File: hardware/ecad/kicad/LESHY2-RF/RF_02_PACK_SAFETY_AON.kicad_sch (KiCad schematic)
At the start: 0 parts

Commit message: complete exact H2.3.1 RF power hierarchy
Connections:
- no-connect marks 0 -> 7
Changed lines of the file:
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@@
 	(generator_version "10.0")
 	(paper "A4")
+	(hierarchical_label "PACK_ADMISSION_VDD"
+		(shape bidirectional)
+		(at 20.32 20.32 0)
+		(effects (font (size 1.27 1.27)))
+	)
+	(wire
+		(pts (xy 20.32 20.32) (xy 25.40 20.32))
+		(stroke (width 0) (type default))
+	)
+	(no_connect (at 25.40 20.32)
+	)
+	(hierarchical_label "POWER_COMMAND_OFF_N"
+		(shape bidirectional)
+		(at 20.32 25.40 0)
+		(effects (font (size 1.27 1.27)))
+	)
+	(wire
+		(pts (xy 20.32 25.40) (xy 25.40 25.40))
+		(stroke (width 0) (type default))
+	)
+	(no_connect (at 25.40 25.40)
+	)
+	(hierarchical_label "POWER_GROUND"
+		(shape bidirectional)
+		(at 20.32 30.48 0)
+		(effects (font (size 1.27 1.27)))
+	)
+	(wire
+		(pts (xy 20.32 30.48) (xy 25.40 30.48))
+		(stroke (width 0) (type default))
+	)
+	(no_connect (at 25.40 30.48)
+	)
+	(hierarchical_label "PROTECTED_PACK_POSITIVE"
+		(shape bidirectional)
+		(at 20.32 35.56 0)
+		(effects (font (size 1.27 1.27)))
+	)
+	(wire
+		(pts (xy 20.32 35.56) (xy 25.40 35.56))
+		(stroke (width 0) (type default))
+	)
+	(no_connect (at 25.40 35.56)
+	)
+	(hierarchical_label "SYS_I2C_SCL"
+		(shape bidirectional)
+		(at 190.50 20.32 180)
+		(effects (font (size 1.27 1.27)) (justify right))
+	)
+	(wire
+		(pts (xy 190.50 20.32) (xy 185.42 20.32))
+		(stroke (width 0) (type default))
+	)
+	(no_connect (at 185.42 20.32)
+	)
+	(hierarchical_label "SYS_I2C_SDA"
+		(shape bidirectional)
+		(at 190.50 25.40 180)
+		(effects (font (size 1.27 1.27)) (justify right))
+	)
+	(wire
+		(pts (xy 190.50 25.40) (xy 185.42 25.40))
+		(stroke (width 0) (type default))
+	)
+	(no_connect (at 185.42 25.40)
+	)
+	(hierarchical_label "SYS_INT_N"
+		(shape bidirectional)
+		(at 190.50 30.48 180)
+		(effects (font (size 1.27 1.27)) (justify right))
+	)
+	(wire
+		(pts (xy 190.50 30.48) (xy 185.42 30.48))
+		(stroke (width 0) (type default))
+	)
+	(no_connect (at 185.42 30.48)
+	)
 	(sheet_instances
 		(path "/"

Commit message: complete exact H2.3.3 pack safety
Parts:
- added BT1: Keystone Electronics 1048P, Leshy2:Keystone-1048P, symbol Leshy2:RF02_PACK_HOLDER
- added BT2: XTAR 18650 4000mAh, symbol Leshy2:RF02_PACK_CELL0
- added BT3: XTAR 18650 4000mAh, symbol Leshy2:RF02_PACK_CELL1
- added C1: TDK C1005X7R1H104K050BB, Capacitor_SMD:C_0402_1005Metric, symbol Leshy2:RF02_PACK_IN_BYPASS
- added C10: Murata GRM188R60J106ME47D, Capacitor_SMD:C_0603_1608Metric, symbol Leshy2:RF02_PACK_ADMISSION_BULK_CAP
- added C11: TDK C1005X7R1H104K050BB, Capacitor_SMD:C_0402_1005Metric, symbol Leshy2:RF02_PACK_ADMISSION_BYPASS
- added C12: Murata GRM155R71H103KA88D, Capacitor_SMD:C_0402_1005Metric, symbol Leshy2:RF02_PACK_ADMISSION_RESET_CAP
- added C13: Murata GRM31C5C1H224JE02L, Capacitor_SMD:C_1206_3216Metric, symbol Leshy2:RF02_PACK_DIAG_TIMER_CAP
- added C14: TDK C1608X7R1C105K080AC, Capacitor_SMD:C_0603_1608Metric, symbol Leshy2:RF02_PACK_DIAG_LOCKOUT_CAP
- added C15: TDK C1005X7R1H104K050BB, Capacitor_SMD:C_0402_1005Metric, symbol Leshy2:RF02_PACK_DIAG_TIMER_BYPASS
- added C16: Murata GRM155R71H103KA88D, Capacitor_SMD:C_0402_1005Metric, symbol Leshy2:RF02_PACK_MID_ADC_FILTER
- added C17: Murata GRM155R71H103KA88D, Capacitor_SMD:C_0402_1005Metric, symbol Leshy2:RF02_PACK_STACK_ADC_FILTER
- added C2: Murata GRM188R71E474KA12D, Capacitor_SMD:C_0603_1608Metric, symbol Leshy2:RF02_PACK_CP_CAP
- added C3: TDK C1005X7R1H104K050BB, Capacitor_SMD:C_0402_1005Metric, symbol Leshy2:RF02_PACK_CHG_GATE_CAP
- added C4: TDK C1005X7R1H104K050BB, Capacitor_SMD:C_0402_1005Metric, symbol Leshy2:RF02_PACK_DIS_GATE_CAP
- added C5: Murata GRM188R71E474KA12D, Capacitor_SMD:C_0603_1608Metric, symbol Leshy2:RF02_PACK_AOLDO_CAP
- added C6: Murata GRM188R71E474KA12D, Capacitor_SMD:C_0603_1608Metric, symbol Leshy2:RF02_PACK_REG3_CAP
- added C7: Murata GRM188R71E474KA12D, Capacitor_SMD:C_0603_1608Metric, symbol Leshy2:RF02_PACK_REG2_CAP
- added C8: TDK C1005X7R1H104K050BB, Capacitor_SMD:C_0402_1005Metric, symbol Leshy2:RF02_PACK_CELL1_FILTER_CAP
- added C9: TDK C1005X7R1H104K050BB, Capacitor_SMD:C_0402_1005Metric, symbol Leshy2:RF02_PACK_BATTS_FILTER_CAP
- added D1: onsemi BAV70LT1G, Package_TO_SOT_SMD:SOT-23, symbol Leshy2:RF02_PACK_SUPPLY_OR
- added D2: Diodes Incorporated BAT54-7-F, Package_TO_SOT_SMD:SOT-23, symbol Leshy2:RF02_PACK_SYSTEM_DIODE
- added F1: Littelfuse 0451005.MRL, Leshy2:0451005.MRL, symbol Leshy2:RF02_PACK_FUSE0
- added F2: Littelfuse 0451005.MRL, Leshy2:0451005.MRL, symbol Leshy2:RF02_PACK_FUSE1
- added Q1: Diodes Incorporated 2N7002DW-7-F, Package_TO_SOT_SMD:SOT-363_SC-70-6, symbol Leshy2:RF02_PACK_HOLD
- added Q2: Diodes Incorporated 2N7002DW-7-F, Package_TO_SOT_SMD:SOT-363_SC-70-6, symbol Leshy2:RF02_PACK_STATUS_BUFFER
- added Q3: Diodes Incorporated DMN2056U-7, Package_TO_SOT_SMD:SOT-23, symbol Leshy2:RF02_PACK_DIAG_SWITCH
- added R1: Vishay WSL25125L000FEA, Resistor_SMD:R_2512_6332Metric, symbol Leshy2:RF02_PACK_SHUNT
- added R10: Yageo RC0402FR-071KL, Resistor_SMD:R_0402_1005Metric, symbol Leshy2:RF02_PACK_PCKP_RES
- added R11: Panasonic ERJ-P08F49R9V, Resistor_SMD:R_1206_3216Metric, symbol Leshy2:RF02_PACK_CELL1_RBAL
- added R12: Panasonic ERJ-P08F49R9V, Resistor_SMD:R_1206_3216Metric, symbol Leshy2:RF02_PACK_BATTS_RBAL
- added R13: Yageo RC0402FR-0747KL, Resistor_SMD:R_0402_1005Metric, symbol Leshy2:RF02_PACK_ADMISSION_RESET_PULLUP
- added R14: Yageo RC0402FR-07169KL, Resistor_SMD:R_0402_1005Metric, symbol Leshy2:RF02_PACK_DIAG_TIMER_RES
- added R15: Yageo RC0402FR-07620KL, Resistor_SMD:R_0402_1005Metric, symbol Leshy2:RF02_PACK_DIAG_LOCKOUT_RES
- added R16: Yageo RC0402FR-0710KL, Resistor_SMD:R_0402_1005Metric, symbol Leshy2:RF02_PACK_DIAG_TRIGGER_PULLDOWN
- added R17: Yageo RC0402FR-0710KL, Resistor_SMD:R_0402_1005Metric, symbol Leshy2:RF02_PACK_DIAG_GATE_PULLDOWN
- added R18: Bourns CRM2512-FX-20R0ELF, Resistor_SMD:R_2512_6332Metric, symbol Leshy2:RF02_PACK_DIAG_RES0
- added R19: Bourns CRM2512-FX-20R0ELF, Resistor_SMD:R_2512_6332Metric, symbol Leshy2:RF02_PACK_DIAG_RES1
- added R2: Yageo RC0402FR-0710KL, Resistor_SMD:R_0402_1005Metric, symbol Leshy2:RF02_PACK_HOLD_PULLUP
- added R20: Yageo RC0402FR-07220KL, Resistor_SMD:R_0402_1005Metric, symbol Leshy2:RF02_PACK_MID_ADC_TOP0
- added R21: Yageo RC0402FR-07220KL, Resistor_SMD:R_0402_1005Metric, symbol Leshy2:RF02_PACK_MID_ADC_TOP1
- added R22: Yageo RC0402FR-07169KL, Resistor_SMD:R_0402_1005Metric, symbol Leshy2:RF02_PACK_MID_ADC_BOTTOM
- added R23: Yageo RC0402FR-07220KL, Resistor_SMD:R_0402_1005Metric, symbol Leshy2:RF02_PACK_STACK_ADC_TOP0
- added R24: Yageo RC0402FR-07220KL, Resistor_SMD:R_0402_1005Metric, symbol Leshy2:RF02_PACK_STACK_ADC_TOP1
- added R25: Yageo RC0402FR-07220KL, Resistor_SMD:R_0402_1005Metric, symbol Leshy2:RF02_PACK_STACK_ADC_TOP2
- added R26: Yageo RC0402FR-07220KL, Resistor_SMD:R_0402_1005Metric, symbol Leshy2:RF02_PACK_STACK_ADC_TOP3
- added R27: Yageo RC0402FR-07220KL, Resistor_SMD:R_0402_1005Metric, symbol Leshy2:RF02_PACK_STACK_ADC_TOP4
- added R28: Yageo RC0402FR-07169KL, Resistor_SMD:R_0402_1005Metric, symbol Leshy2:RF02_PACK_STACK_ADC_BOTTOM
- added R3: Yageo RC0402FR-0710KL, Resistor_SMD:R_0402_1005Metric, symbol Leshy2:RF02_PACK_HOLD_RELEASE_PULLDOWN
- added R4: Yageo RC0402FR-0710KL, Resistor_SMD:R_0402_1005Metric, symbol Leshy2:RF02_PACK_ALRT_PULLUP
- added R5: Yageo RC0402FR-0710KL, Resistor_SMD:R_0402_1005Metric, symbol Leshy2:RF02_PACK_PFAIL_PULLUP
- added R6: Yageo RC0402FR-0710KL, Resistor_SMD:R_0402_1005Metric, symbol Leshy2:RF02_PACK_IRQ_GATE_PULLDOWN
- added R7: Yageo RC0402FR-0710KL, Resistor_SMD:R_0402_1005Metric, symbol Leshy2:RF02_PACK_GAUGE_SCL_PULLUP
- added R8: Yageo RC0402FR-0710KL, Resistor_SMD:R_0402_1005Metric, symbol Leshy2:RF02_PACK_GAUGE_SDA_PULLUP
- added R9: Panasonic ERJ-P08F10R0V, Resistor_SMD:R_1206_3216Metric, symbol Leshy2:RF02_PACK_IN_RES
- added RT1: TDK B57332V5103F360, Capacitor_SMD:C_0603_1608Metric, symbol Leshy2:RF02_PACK_NTC0
- added RT2: TDK B57332V5103F360, Capacitor_SMD:C_0603_1608Metric, symbol Leshy2:RF02_PACK_NTC1
- added U1: Analog Devices MAX17320G20+T, Package_DFN_QFN:TQFN-24-1EP_4x4mm_P0.5mm_EP2.6x2.6mm, symbol Leshy2:RF02_PACK_GAUGE
- added U2: Texas Instruments MSPM0C1106SDGS20R, Package_SO:Texas_DGS0020A_TSSOP-20_3x5.1mm_P0.5mm, symbol Leshy2:RF02_PACK_ADMISSION
- added U3: Texas Instruments CSD87313DMST, Leshy2:CSD87313DMST, symbol Leshy2:RF02_PACK_POWER_FET
- added U4: Texas Instruments TPUL2G223BQBR, Leshy2:TPUL2G223BQBR, symbol Leshy2:RF02_PACK_DIAG_TIMER
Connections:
- net PACK_ADMISSION_VDD: now also C10.1 (END_1), C11.1 (END_1), C15.1 (END_1), D1.3 (K_COMMON), D2.3 (K), R13.1 (END_1), R14.1 (END_1), R15.1 (END_1), R5.1 (END_1), R7.1 (END_1), R8.1 (END_1), U2.6 (VDD), U4.10 (CH2_T), U4.11 (CH2_CLR_N), U4.16 (VCC)
- net POWER_COMMAND_OFF_N: now also U2.19 (PA24)
- net POWER_GROUND: now also R1.2 (END_2), U1.14 (CSN)
- net PROTECTED_PACK_POSITIVE: now also C4.2 (END_2), R10.2 (END_2), U3.5 (S2_5), U3.6 (S2_6)
- net SYS_I2C_SCL: now also U2.11 (PA11)
- net SYS_I2C_SDA: now also U2.4 (PA0)
- net SYS_INT_N: now also Q2.1 (D2)
- new net 3V3_MAIN: D2.1 (A)
- new net BATTERY_STACK_POSITIVE: C3.2 (END_2), F2.2 (END_2), R12.1 (END_1), R18.1 (END_1), R19.1 (END_1), R23.1 (END_1), R9.1 (END_1), U3.7 (S1_7), U3.8 (S1_8)
- new net PACK_2S_MIDPOINT: BT1.4 (SLOT1_NEG), BT3.2 (NEG), F1.2 (END_2), R11.1 (END_1), R20.1 (END_1)
- new net PACK_ADMISSION_NRST_N: C12.1 (END_1), R13.2 (END_2), U2.5 (PA1_NRST)
- new net PACK_ADMISSION_SWCLK: U2.16 (PA20_SWCLK)
- new net PACK_ADMISSION_SWDIO: U2.15 (PA19_SWDIO)
- new net PACK_ADMISSION_UART_RX: U2.14 (PA18)
- new net PACK_ADMISSION_UART_TX: U2.13 (PA17)
- new net PACK_AOLDO: C5.1 (END_1), D1.1 (A1), R2.1 (END_1), U1.12 (AOLDO)
- new net PACK_BATTS_SENSE: C9.1 (END_1), R12.2 (END_2), U1.24 (BATTS)
- new net PACK_CELL0_ADC: C16.1 (END_1), R21.2 (END_2), R22.1 (END_1), U2.20 (PA25)
- new net PACK_CELL0_TEMP: RT1.1 (END_1), U1.10 (TH1)
- new net PACK_CELL1_SENSE: C8.1 (END_1), C9.2 (END_2), R11.2 (END_2), U1.21 (CELL1), U1.22 (CELL2), U1.23 (CELL3)
- new net PACK_CELL1_TEMP: RT2.1 (END_1), U1.16 (TH2)
- new net PACK_CHARGE_PUMP: C2.1 (END_1), U1.2 (CP)
- new net PACK_CHG_GATE: C3.1 (END_1), U1.3 (CHG), U3.1 (G1)
- new net PACK_DIAG_GATE: Q3.1 (G), R17.1 (END_1), U4.13 (CH1_Q), U4.9 (CH2_T_N)
- new net PACK_DIAG_LOAD_DRAIN: Q3.3 (D), R18.2 (END_2), R19.2 (END_2)
- new net PACK_DIAG_LOCKOUT_RC: C14.1 (END_1), R15.2 (END_2), U4.7 (CH2_RC)
- new net PACK_DIAG_REFRACTORY_CLEAR_N: U4.12 (CH2_Q_N), U4.3 (CH1_CLR_N)
- new net PACK_DIAG_TIMER_RC: C13.1 (END_1), R14.2 (END_2), U4.15 (CH1_RC)
- new net PACK_DIAG_TRIGGER: R16.1 (END_1), U2.17 (PA22), U4.2 (CH1_T)
- new net PACK_DIS_GATE: C4.1 (END_1), U1.4 (DIS), U3.4 (G2)
- new net PACK_FET_COMMON_DRAIN: U3.2 (D_COMMON_2), U3.3 (D_COMMON_3), U3.9 (D_COMMON_EP)
- new net PACK_FET_HOLD_RELEASE: Q1.5 (G2), R3.1 (END_1), U2.10 (PA6)
- new net PACK_FET_OVERRIDE_N: Q1.4 (D1), R4.2 (END_2), U1.7 (ALRT)
- new net PACK_FIXTURE_3V3: D1.2 (A2)
- new net PACK_GAUGE_I2C_SCL: R7.2 (END_2), U1.8 (SCL_OD), U2.8 (PA2)
- new net PACK_GAUGE_I2C_SDA: R8.2 (END_2), U1.9 (SDA_DQ), U2.9 (PA4)
- new net PACK_GAUGE_IN: C1.1 (END_1), C2.2 (END_2), R9.2 (END_2), U1.1 (IN)
- new net PACK_HOLD_GATE: Q1.1 (D2), Q1.2 (G1), R2.2 (END_2)
- new net PACK_LOCAL_GND: BT1.2 (SLOT0_NEG), BT2.2 (NEG), C1.2 (END_2), C10.2 (END_2), C11.2 (END_2), C12.2 (END_2), C13.2 (END_2), C14.2 (END_2), C15.2 (END_2), C16.2 (END_2), C17.2 (END_2), C5.2 (END_2), C6.2 (END_2), C7.2 (END_2), C8.2 (END_2), Q1.3 (S1), Q1.6 (S2), Q2.3 (S1), Q2.6 (S2), Q3.2 (S), R1.1 (END_1), R16.2 (END_2), R17.2 (END_2), R22.2 (END_2), R28.2 (END_2), R3.2 (END_2), R6.2 (END_2), RT1.2 (END_2), RT2.2 (END_2), U1.15 (CSP), U1.18 (TH3), U1.19 (TH4), U1.20 (GND), U1.25 (EP_GND), U2.7 (VSS), U4.1 (CH1_T_N), U4.14 (CH1_C), U4.17 (GND_EP), U4.6 (CH2_C), U4.8 (GND)
- new net PACK_MID_DIV_SERIES: R20.2 (END_2), R21.1 (END_1)
- new net PACK_PCKP_SENSE: R10.1 (END_1), U1.6 (PCKP)
- new net PACK_PFAIL_N: Q2.4 (D1), R5.2 (END_2), U2.12 (PA16)
- new net PACK_PFAIL_RAW: Q2.2 (G1), U1.11 (PFAIL)
- new net PACK_REG2_1V8: C7.1 (END_1), U1.17 (REG2)
- new net PACK_REG3_3V4: C6.1 (END_1), R4.1 (END_1), U1.13 (REG3)
- new net PACK_SLOT0_POSITIVE_RAW: BT1.1 (SLOT0_POS), BT2.1 (POS), F1.1 (END_1)
- new net PACK_SLOT1_POSITIVE_RAW: BT1.3 (SLOT1_POS), BT3.1 (POS), F2.1 (END_1)
- new net PACK_STACK_ADC: C17.1 (END_1), R27.2 (END_2), R28.1 (END_1), U2.1 (PA26)
- new net PACK_STACK_DIV_SERIES_01: R23.2 (END_2), R24.1 (END_1)
- new net PACK_STACK_DIV_SERIES_12: R24.2 (END_2), R25.1 (END_1)
- new net PACK_STACK_DIV_SERIES_23: R25.2 (END_2), R26.1 (END_1)
- new net PACK_STACK_DIV_SERIES_34: R26.2 (END_2), R27.1 (END_1)
- new net PACK_SYS_INT_REQ: Q2.5 (G2), R6.1 (END_1), U2.18 (PA23)
- no-connect marks 7 -> 6
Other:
- title: (none) -> Leshy2 — exact fail-closed 2S pack admission and diagnostics

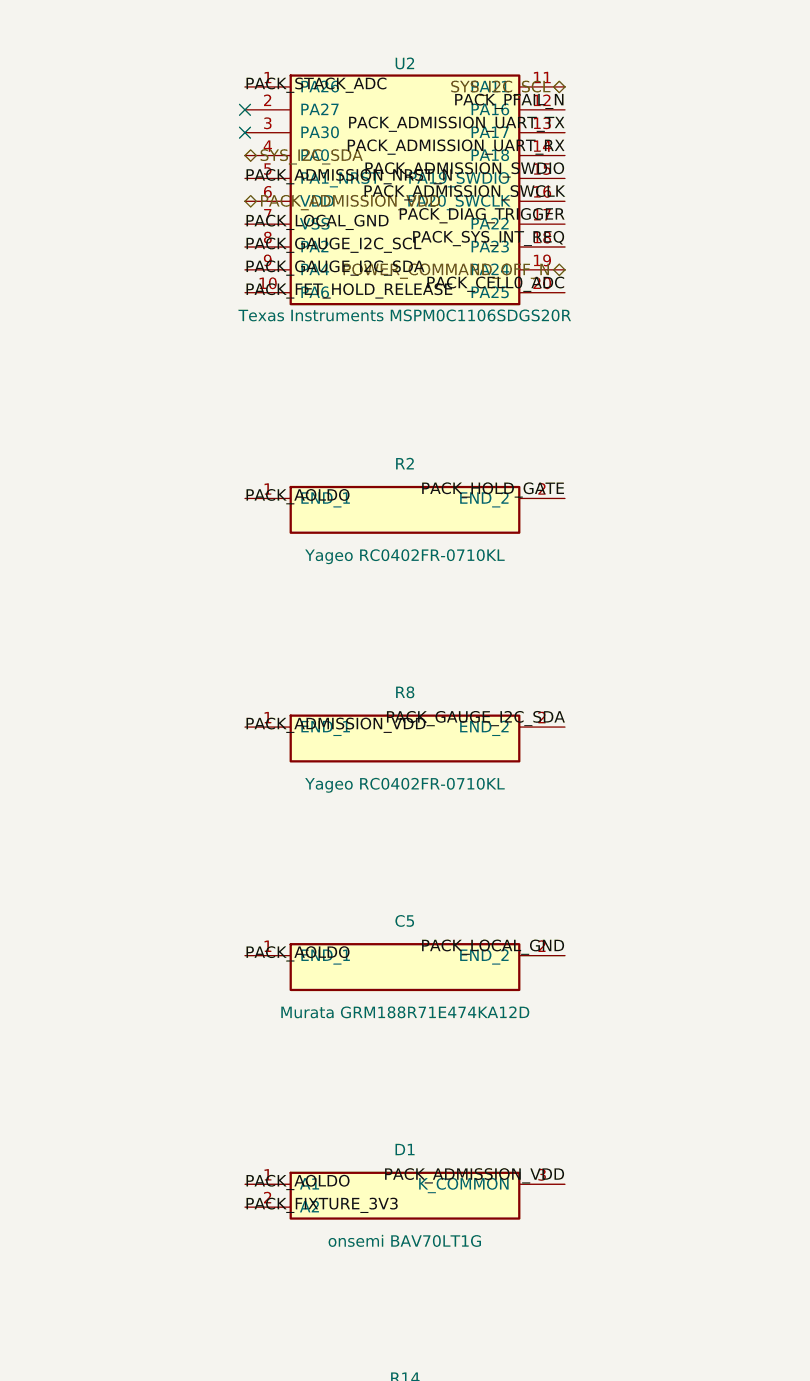
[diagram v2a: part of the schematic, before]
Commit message: complete exact H2.3.13 RF testpoint sheet
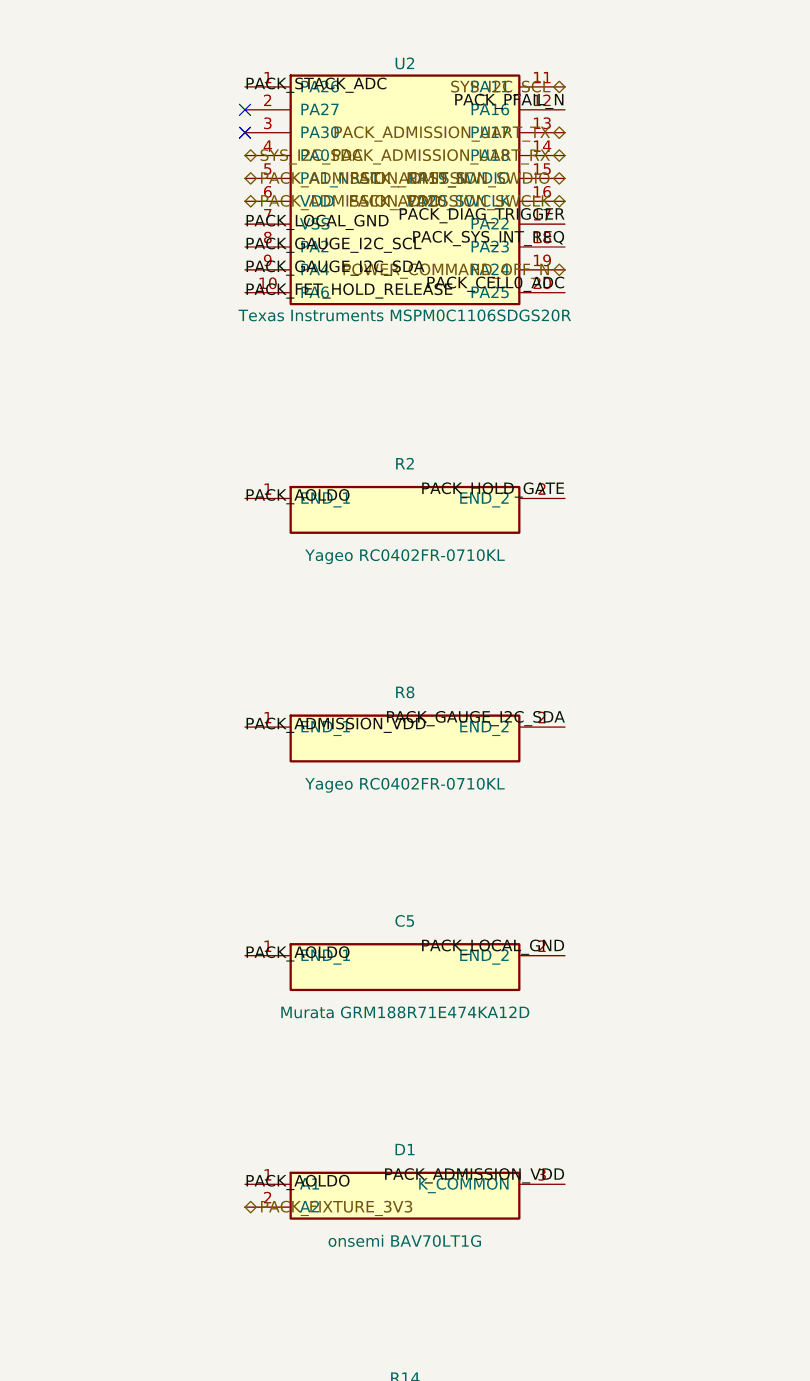
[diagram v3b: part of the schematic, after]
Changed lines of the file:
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@@
 		(effects (font (size 1.27 1.27)))
 	)
-	(label "PACK_ADMISSION_NRST_N"
+	(hierarchical_label "PACK_ADMISSION_NRST_N"
+		(shape bidirectional)
 		(at 114.30 55.88 0)
 		(effects (font (size 1.27 1.27)))
@@
 		(effects (font (size 1.27 1.27)))
 	)
-	(label "PACK_ADMISSION_SWCLK"
+	(hierarchical_label "PACK_ADMISSION_SWCLK"
+		(shape bidirectional)
 		(at 149.86 58.42 180)
 		(effects (font (size 1.27 1.27)) (justify right bottom))
 	)
-	(label "PACK_ADMISSION_SWDIO"
+	(hierarchical_label "PACK_ADMISSION_SWDIO"
+		(shape bidirectional)
 		(at 149.86 55.88 180)
 		(effects (font (size 1.27 1.27)) (justify right bottom))
 	)
-	(label "PACK_ADMISSION_UART_RX"
+	(hierarchical_label "PACK_ADMISSION_UART_RX"
+		(shape bidirectional)
 		(at 149.86 53.34 180)
 		(effects (font (size 1.27 1.27)) (justify right bottom))
 	)
-	(label "PACK_ADMISSION_UART_TX"
+	(hierarchical_label "PACK_ADMISSION_UART_TX"
+		(shape bidirectional)
 		(at 149.86 50.80 180)
 		(effects (font (size 1.27 1.27)) (justify right bottom))
@@
 		(effects (font (size 1.27 1.27)) (justify right bottom))
 	)
-	(label "PACK_FIXTURE_3V3"
+	(hierarchical_label "PACK_FIXTURE_3V3"
+		(shape bidirectional)
 		(at 114.30 170.18 0)
 		(effects (font (size 1.27 1.27)))

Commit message: complete H2 schematic review package
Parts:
- renumbered BT1 to BT2001, BT2 to BT2002, BT3 to BT2003, C1 to C2001, C2 to C2002, C3 to C2003, C4 to C2004, C5 to C2005, C6 to C2006, C7 to C2007, C8 to C2008, C9 to C2009, C10 to C2010, C11 to C2011, C12 to C2012, C13 to C2013, C14 to C2014, C15 to C2015, C16 to C2016, C17 to C2017, D1 to D2001, D2 to D2002, F1 to F2001, F2 to F2002, Q1 to Q2001, Q2 to Q2002, Q3 to Q2003, R1 to R2001, R2 to R2002, R3 to R2003, R4 to R2004, R5 to R2005, R6 to R2006, R7 to R2007, R8 to R2008, R9 to R2009, R10 to R2010, R11 to R2011, R12 to R2012, R13 to R2013, R14 to R2014, R15 to R2015, R16 to R2016, R17 to R2017, R18 to R2018, R19 to R2019, R20 to R2020, R21 to R2021, R22 to R2022, R23 to R2023, R24 to R2024, R25 to R2025, R26 to R2026, R27 to R2027, R28 to R2028, RT1 to RT2001, RT2 to RT2002, U1 to U2001, U2 to U2002, U3 to U2003, U4 to U2004

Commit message: Optimize H1 display and stocked BOM routes
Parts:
- C2001, C2003, C2004, C2008, C2009, C2011, C2015: value TDK C1005X7R1H104K050BB -> Yageo CC0402KRX7R9BB104
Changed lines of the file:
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@@
 			(effects (font (size 1.27 1.27)))
 		)
-		(property "Value" "TDK C1005X7R1H104K050BB"
+		(property "Value" "Yageo CC0402KRX7R9BB104"
 			(at 375.92 125.73 0)
 			(show_name no)
@@
 			(effects (font (size 1.27 1.27)))
 		)
-		(property "Value" "TDK C1005X7R1H104K050BB"
+		(property "Value" "Yageo CC0402KRX7R9BB104"
 			(at 457.20 128.27 0)
 			(show_name no)
@@
 			(effects (font (size 1.27 1.27)))
 		)
-		(property "Value" "TDK C1005X7R1H104K050BB"
+		(property "Value" "Yageo CC0402KRX7R9BB104"
 			(at 50.80 130.81 0)
 			(show_name no)
@@
 			(effects (font (size 1.27 1.27)))
 		)
-		(property "Value" "TDK C1005X7R1H104K050BB"
+		(property "Value" "Yageo CC0402KRX7R9BB104"
 			(at 50.80 156.21 0)
 			(show_name no)
@@
 			(effects (font (size 1.27 1.27)))
 		)
-		(property "Value" "TDK C1005X7R1H104K050BB"
+		(property "Value" "Yageo CC0402KRX7R9BB104"
 			(at 213.36 163.83 0)
 			(show_name no)
@@
 			(effects (font (size 1.27 1.27)))
 		)
-		(property "Value" "TDK C1005X7R1H104K050BB"
+		(property "Value" "Yageo CC0402KRX7R9BB104"
 			(at 538.48 176.53 0)
 			(show_name no)
@@
 			(effects (font (size 1.27 1.27)))
 		)
-		(property "Value" "TDK C1005X7R1H104K050BB"
+		(property "Value" "Yageo CC0402KRX7R9BB104"
 			(at 457.20 204.47 0)
 			(show_name no)

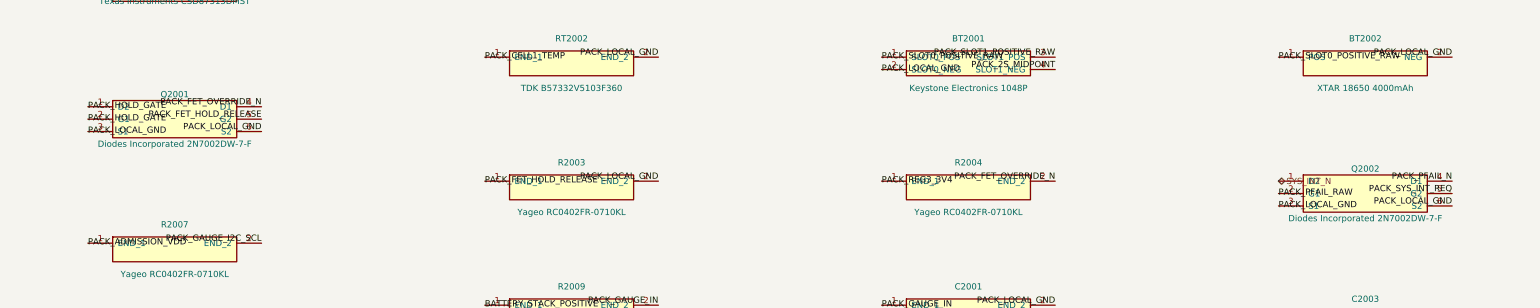
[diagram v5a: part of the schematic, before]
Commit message: Correct dual-NMOS physical pin mapping
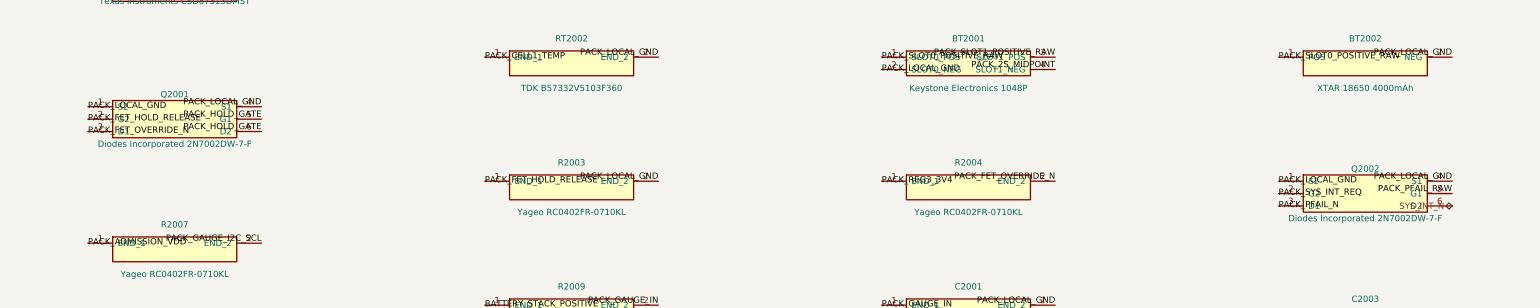
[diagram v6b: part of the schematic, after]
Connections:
- net PACK_FET_HOLD_RELEASE: now also Q2001.2 (G2); no longer Q2001.5 (G2)
- net PACK_FET_OVERRIDE_N: now also Q2001.3 (D1); no longer Q2001.4 (D1)
- net PACK_HOLD_GATE: now also Q2001.5 (G1), Q2001.6 (D2); no longer Q2001.1 (D2), Q2001.2 (G1)
- net PACK_LOCAL_GND: now also Q2001.1 (S2), Q2001.4 (S1), Q2002.1 (S2), Q2002.4 (S1); no longer Q2001.3 (S1), Q2001.6 (S2), Q2002.3 (S1), Q2002.6 (S2)
- net PACK_PFAIL_N: now also Q2002.3 (D1); no longer Q2002.4 (D1)
- net PACK_PFAIL_RAW: now also Q2002.5 (G1); no longer Q2002.2 (G1)
- net PACK_SYS_INT_REQ: now also Q2002.2 (G2); no longer Q2002.5 (G2)
- net SYS_INT_N: now also Q2002.6 (D2); no longer Q2002.1 (D2)
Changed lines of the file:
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@@
 	)
 	(label "PACK_FET_HOLD_RELEASE"
-		(at 231.14 81.28 180)
-		(effects (font (size 1.27 1.27)) (justify right bottom))
+		(at 195.58 81.28 0)
+		(effects (font (size 1.27 1.27)))
 	)
 	(label "PACK_FET_HOLD_RELEASE"
@@
 	)
 	(label "PACK_FET_OVERRIDE_N"
-		(at 231.14 78.74 180)
-		(effects (font (size 1.27 1.27)) (justify right bottom))
+		(at 195.58 83.82 0)
+		(effects (font (size 1.27 1.27)))
 	)
 	(label "PACK_FET_OVERRIDE_N"
@@
 	)
 	(label "PACK_HOLD_GATE"
-		(at 195.58 78.74 0)
-		(effects (font (size 1.27 1.27)))
+		(at 231.14 81.28 180)
+		(effects (font (size 1.27 1.27)) (justify right bottom))
 	)
 	(label "PACK_HOLD_GATE"
-		(at 195.58 81.28 0)
-		(effects (font (size 1.27 1.27)))
+		(at 231.14 83.82 180)
+		(effects (font (size 1.27 1.27)) (justify right bottom))
 	)
 	(label "PACK_HOLD_GATE"
@@
 	)
 	(label "PACK_LOCAL_GND"
-		(at 195.58 83.82 0)
-		(effects (font (size 1.27 1.27)))
-	)
-	(label "PACK_LOCAL_GND"
-		(at 231.14 83.82 180)
+		(at 195.58 78.74 0)
+		(effects (font (size 1.27 1.27)))
+	)
+	(label "PACK_LOCAL_GND"
+		(at 231.14 78.74 180)
 		(effects (font (size 1.27 1.27)) (justify right bottom))
 	)
@@
 	)
 	(label "PACK_LOCAL_GND"
-		(at 439.42 99.06 0)
-		(effects (font (size 1.27 1.27)))
-	)
-	(label "PACK_LOCAL_GND"
-		(at 474.98 99.06 180)
+		(at 439.42 93.98 0)
+		(effects (font (size 1.27 1.27)))
+	)
+	(label "PACK_LOCAL_GND"
+		(at 474.98 93.98 180)
 		(effects (font (size 1.27 1.27)) (justify right bottom))
 	)
@@
 	)
 	(label "PACK_PFAIL_N"
-		(at 474.98 93.98 180)
-		(effects (font (size 1.27 1.27)) (justify right bottom))
+		(at 439.42 99.06 0)
+		(effects (font (size 1.27 1.27)))
 	)
 	(label "PACK_PFAIL_N"
@@
 	)
 	(label "PACK_PFAIL_RAW"
-		(at 439.42 96.52 0)
-		(effects (font (size 1.27 1.27)))
+		(at 474.98 96.52 180)
+		(effects (font (size 1.27 1.27)) (justify right bottom))
 	)
 	(label "PACK_REG2_1V8"
@@
 	)
 	(label "PACK_SYS_INT_REQ"
-		(at 474.98 96.52 180)
-		(effects (font (size 1.27 1.27)) (justify right bottom))
+		(at 439.42 96.52 0)
+		(effects (font (size 1.27 1.27)))
 	)
 	(label "PACK_SYS_INT_REQ"
@@
 	(hierarchical_label "SYS_INT_N"
 		(shape bidirectional)
-		(at 439.42 93.98 0)
-		(effects (font (size 1.27 1.27)))
+		(at 474.98 99.06 180)
+		(effects (font (size 1.27 1.27)) (justify right bottom))
 	)
 	(sheet_instances

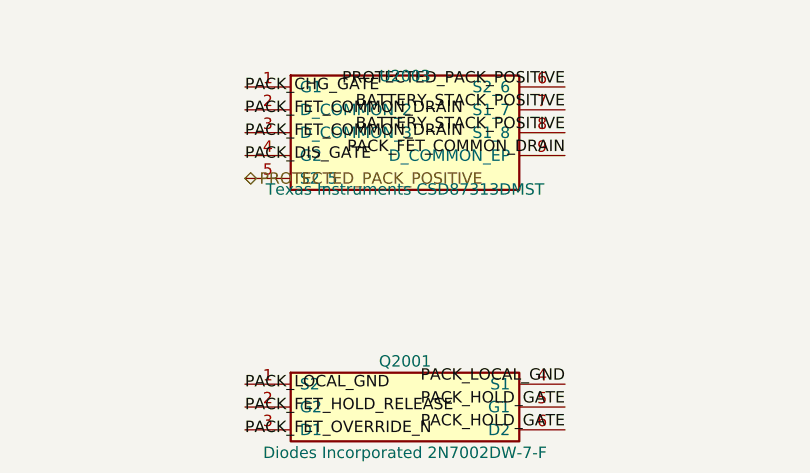
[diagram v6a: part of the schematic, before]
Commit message: Reduce factory BOM cost without functional loss
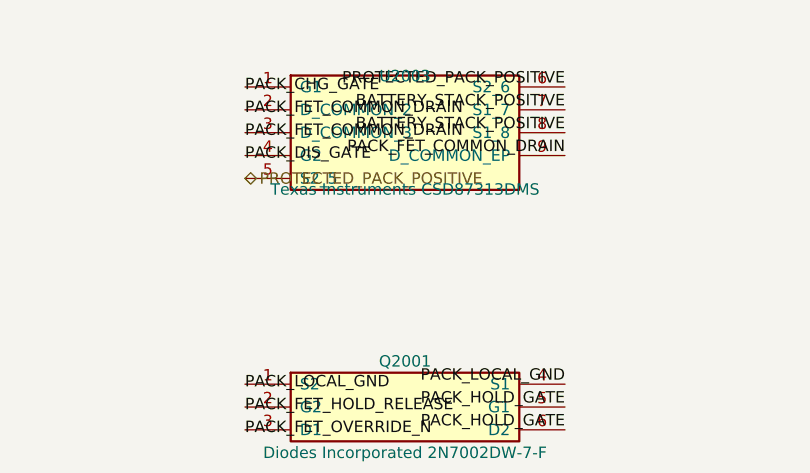
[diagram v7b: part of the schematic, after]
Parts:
- U2003: value Texas Instruments CSD87313DMST -> Texas Instruments CSD87313DMS; footprint Leshy2:CSD87313DMST -> Leshy2:CSD87313DMS
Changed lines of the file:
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@@
 			(effects (font (size 1.27 1.27)))
 		)
-		(property "Value" "Texas Instruments CSD87313DMST"
+		(property "Value" "Texas Instruments CSD87313DMS"
 			(at 213.36 57.10 0)
 			(show_name no)
@@
 			(effects (font (size 1.27 1.27)))
 		)
-		(property "Footprint" "Leshy2:CSD87313DMST"
+		(property "Footprint" "Leshy2:CSD87313DMS"
 			(at 213.36 50.80 0)
 			(show_name no)
